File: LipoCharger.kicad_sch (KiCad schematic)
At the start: 10 parts, among them U1 TP4056-42-ESOP8

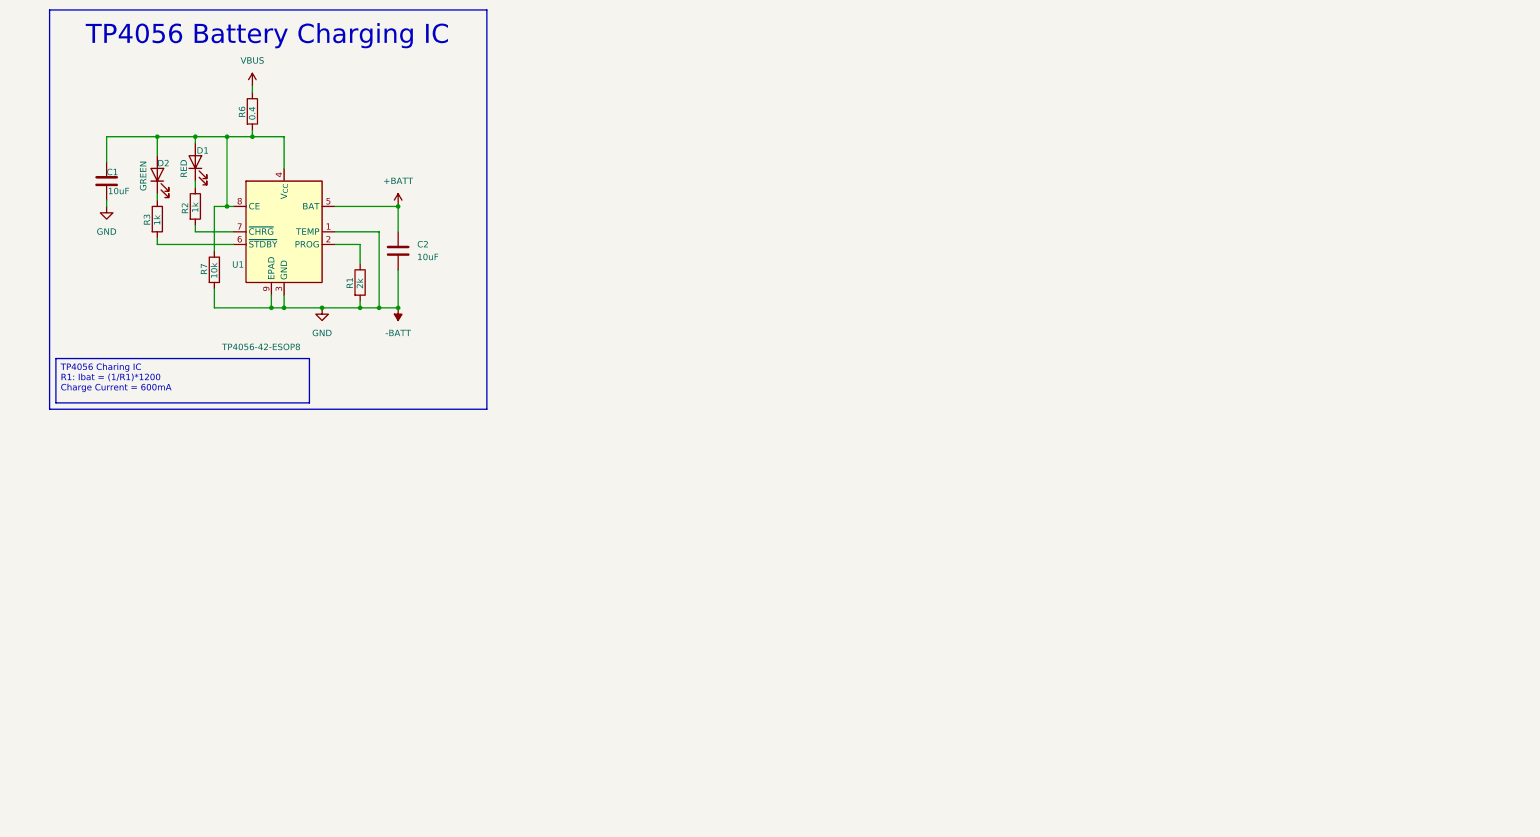
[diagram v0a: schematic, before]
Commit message: Added the DW01 Battery Protection IC and started adding the USB-C port
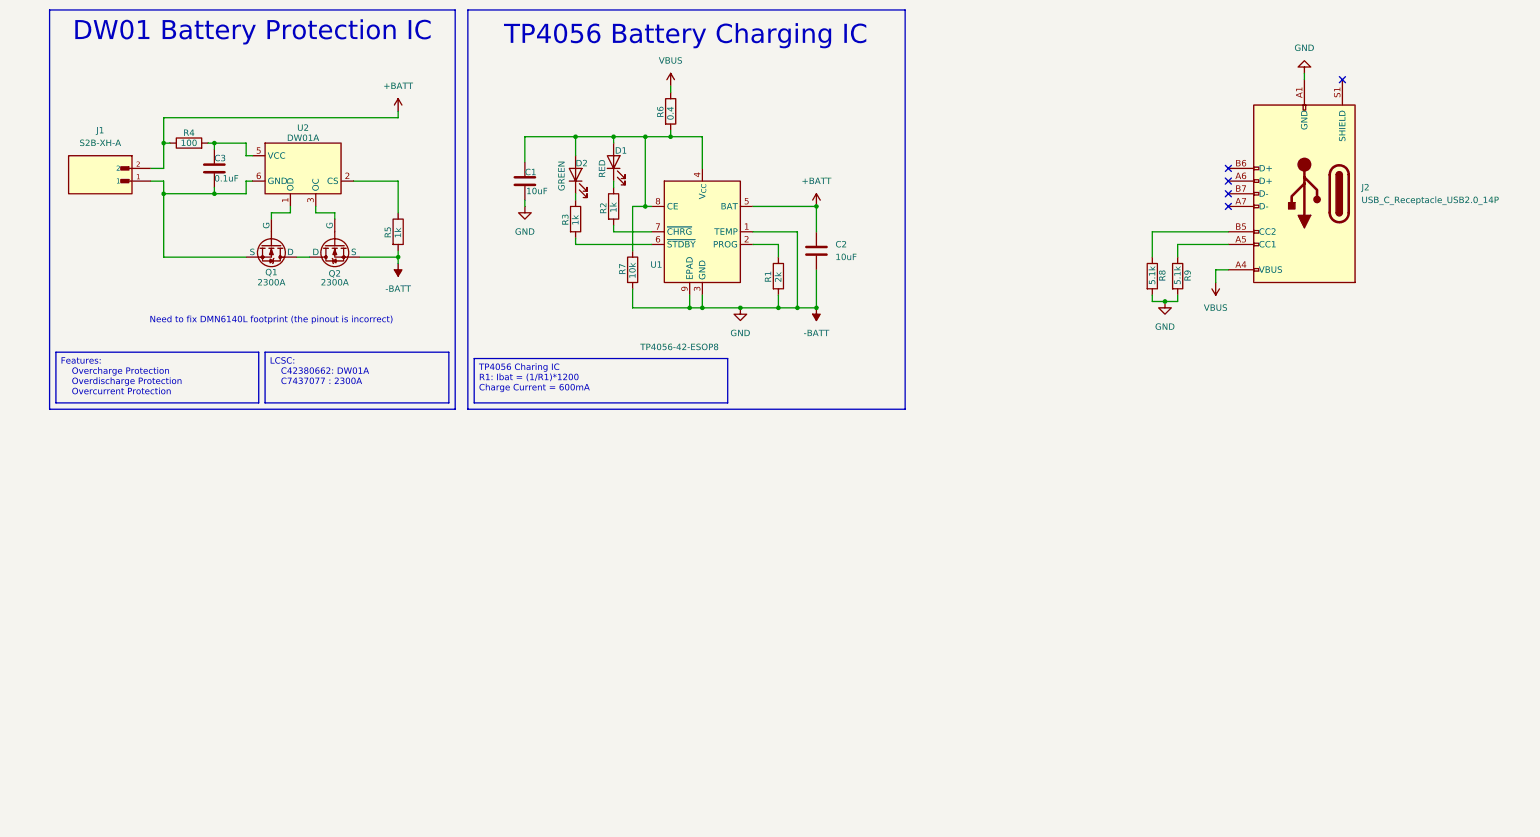
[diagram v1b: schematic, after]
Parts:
- added C3: 0.1uF, Capacitor_SMD:C_0805_2012Metric_Pad1.18x1.45mm_HandSolder, symbol Device:C
- added J1: S2B-XH-A, a_Library:JST_S2B-XH-A, symbol JST_XH:S2B-XH-A
- added J2: USB_C_Receptacle_USB2.0_14P, a_Library:Usb-C, symbol Connector:USB_C_Receptacle_USB2.0_14P
- added Q1, Q2: 2300A, Package_TO_SOT_SMD:SOT-23_Handsoldering, symbol Simulation_SPICE:NMOS
- added R4: 100, Resistor_SMD:R_0805_2012Metric_Pad1.20x1.40mm_HandSolder, symbol Device:R
- added R5: 1k, Resistor_SMD:R_0805_2012Metric_Pad1.20x1.40mm_HandSolder, symbol Device:R
- added R8, R9: 5.1k, Resistor_SMD:R_0805_2012Metric_Pad1.20x1.40mm_HandSolder, symbol Device:R
- added U2: DW01A, Package_TO_SOT_SMD:SOT-23-6, symbol Battery_Management:DW01A
- C1, C2: footprint (none) -> Capacitor_SMD:C_0805_2012Metric_Pad1.18x1.45mm_HandSolder
- R1, R2, R3, R6, R7: footprint (none) -> Resistor_SMD:R_0805_2012Metric_Pad1.20x1.40mm_HandSolder
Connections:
- net +BATT: now also J1.2, R4.1
- net -BATT: now also J2.A1 (GND), J2.A12 (GND), J2.B1 (GND), J2.B12 (GND), Q2.3 (S), R5.2, R8.2, R9.2
- net VBUS: now also J2.A4 (VBUS), J2.A9 (VBUS), J2.B4 (VBUS), J2.B9 (VBUS)
- new net: Q1.1 (D), Q2.1 (D)
- new net: Q2.2 (G), U2.3 (OC)
- new net: C3.2, J1.1, Q1.3 (S), U2.6 (GND)
- new net: C3.1, R4.2, U2.5 (VCC)
- new net: J2.B5 (CC2), R8.1
- new net: J2.A5 (CC1), R9.1
- new net: Q1.2 (G), U2.1 (OD)
- new net: R5.1, U2.2 (CS)
- no-connect marks 0 -> 5
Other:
- note added: "DW01 Battery Protection IC"
- note added: "Need to fix DMN6140L footprint (the pinout is incorrect)"
- moved on the sheet: C1, C2, D1, D2, R1, R2, R3, R6, R7, U1

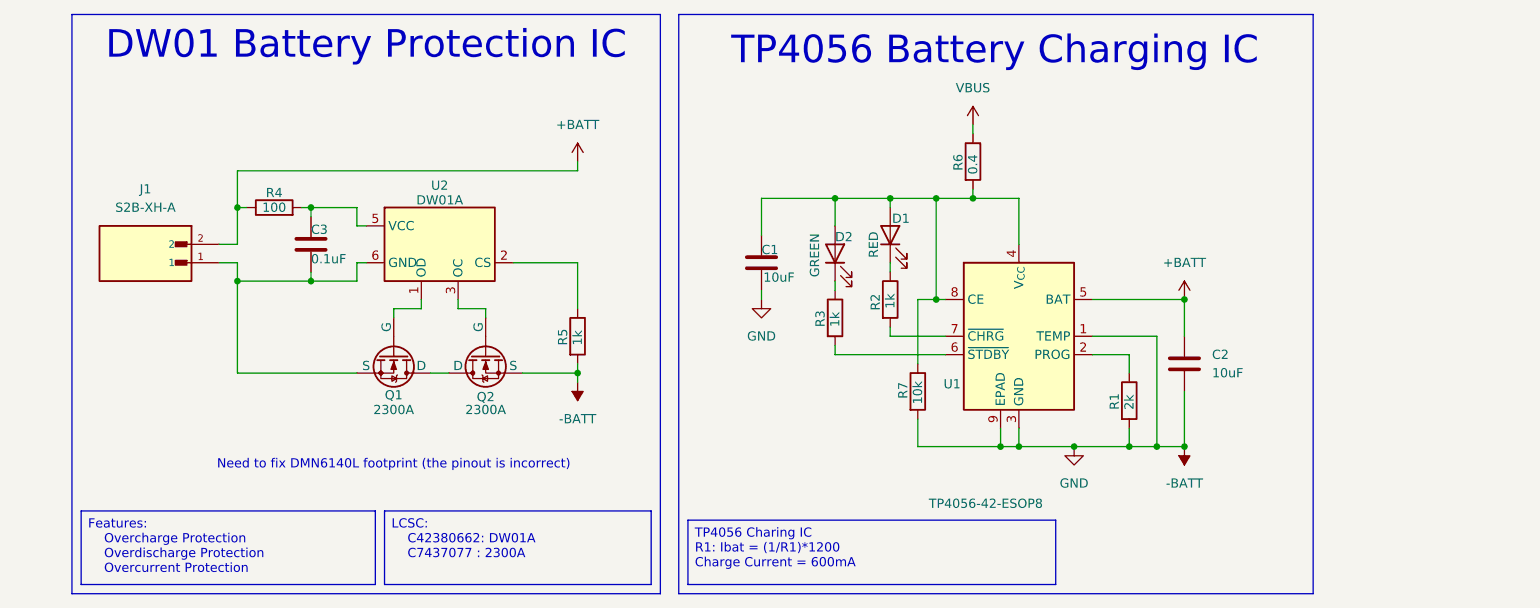
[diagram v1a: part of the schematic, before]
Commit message: Replaced the DW01 with a FM2113
The DW01 was not suited for a LIPO battery, the under voltage threshold was too low, so it was replaced with the FM2113 which has a much higher threshold
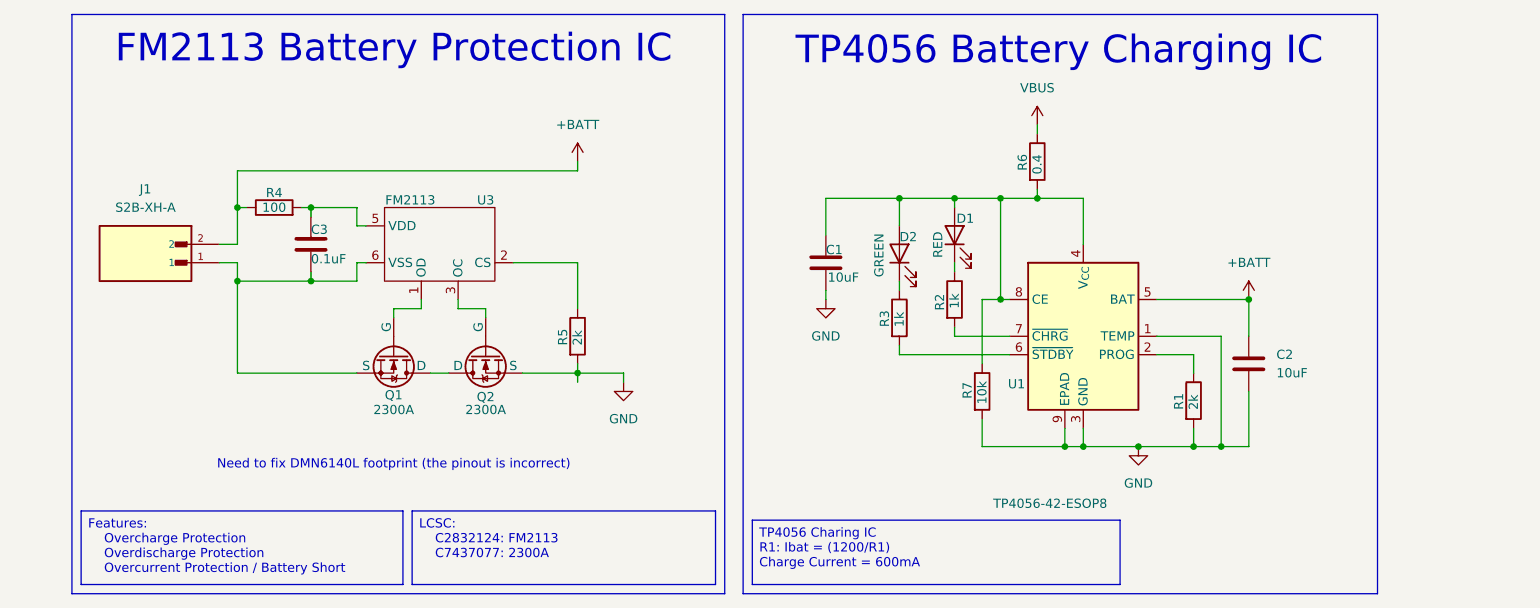
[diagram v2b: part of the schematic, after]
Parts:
- removed U2: DW01A, Package_TO_SOT_SMD:SOT-23-6, symbol Battery_Management:DW01A
- added U3: FM2113, Package_TO_SOT_SMD:TSOT-23-6_HandSoldering, symbol New_Library:FM2113
- R5: value 1k -> 2k
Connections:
- net at Q2.2 (G): now also U3.3 (OC)
- net at C3.2, J1.1, Q1.3 (S): now also U3.6 (VSS)
- net at C3.1, R4.2: now also U3.5 (VDD)
- net at Q1.2 (G): now also U3.1 (OD)
- net at R5.1: now also U3.2 (CS)
- net -BATT renamed GND
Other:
- note added: "FM2113 Battery Protection IC"
- note removed: "DW01 Battery Protection IC"
- moved on the sheet: C1, C2, D1, D2, R1, R2, R3, R6, R7, U1

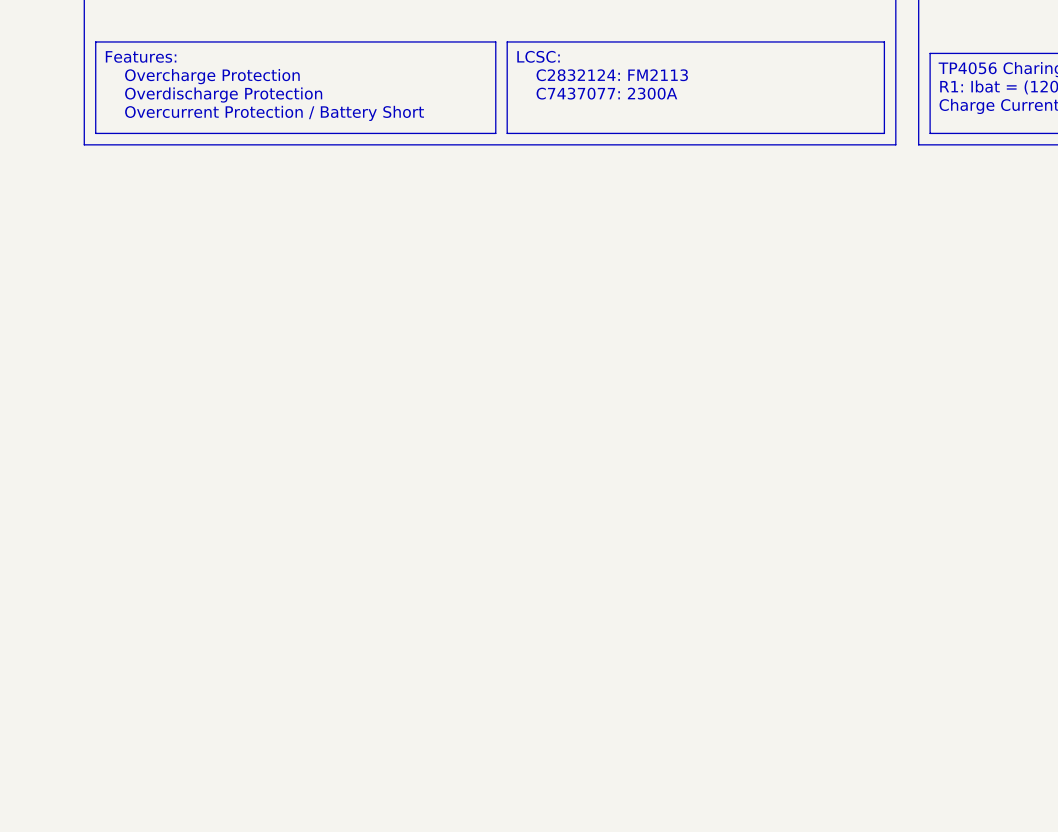
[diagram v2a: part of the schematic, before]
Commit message: Updated usb-c connector, added the 5v switcher, and started to find specific components for the swithcher
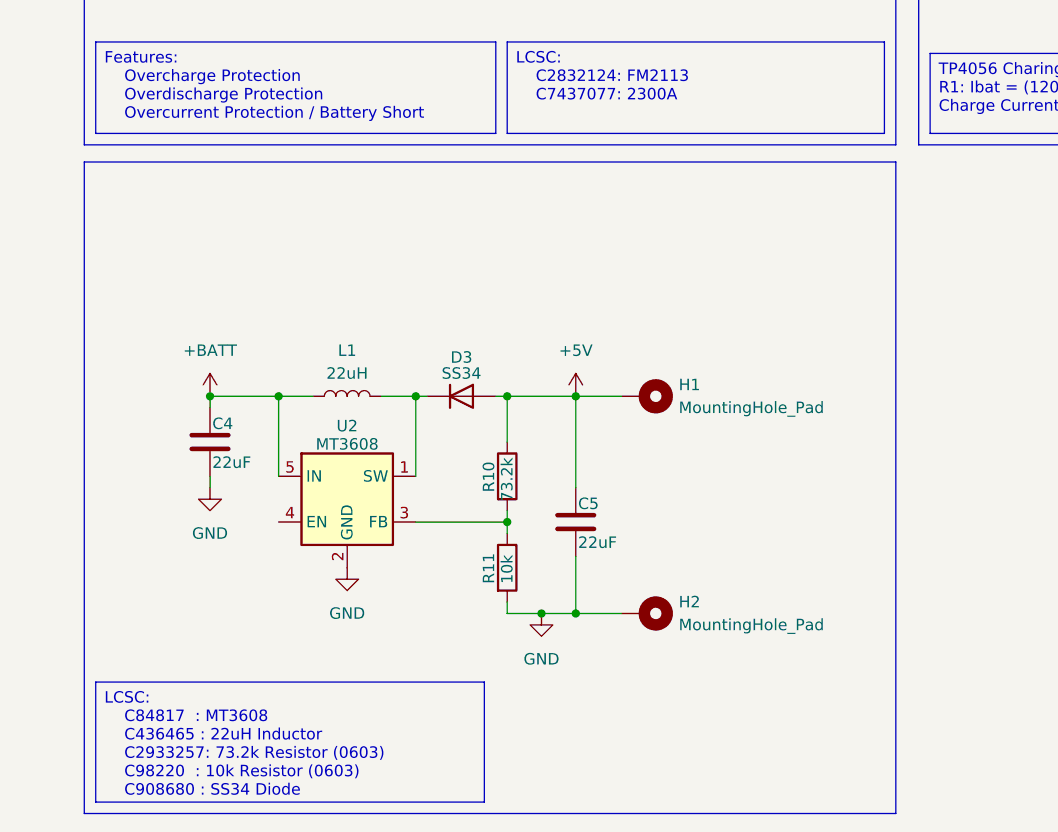
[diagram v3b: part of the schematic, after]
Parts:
- added C4, C5: 22uF, Capacitor_SMD:C_0603_1608Metric_Pad1.08x0.95mm_HandSolder, symbol Device:C
- added D3: SS34, Diode_SMD:D_SMA-SMB_Universal_Handsoldering, symbol Device:D
- added H1, H2: MountingHole_Pad, MountingHole:MountingHole_2.2mm_M2_DIN965_Pad, symbol Mechanical:MountingHole_Pad
- added L1: 22uH, symbol Device:L
- added R10: 73.2k, Resistor_SMD:R_0603_1608Metric_Pad0.98x0.95mm_HandSolder, symbol Device:R
- added R11: 10k, Resistor_SMD:R_0603_1608Metric_Pad0.98x0.95mm_HandSolder, symbol Device:R
- added U2: MT3608, Package_TO_SOT_SMD:SOT-23-6, symbol Regulator_Switching:MT3608
- C1, C2, C3: footprint Capacitor_SMD:C_0805_2012Metric_Pad1.18x1.45mm_HandSolder -> Capacitor_SMD:C_0603_1608Metric_Pad1.08x0.95mm_HandSolder
- D1, D2: footprint (none) -> LED_SMD:LED_0603_1608Metric_Pad1.05x0.95mm_HandSolder
- R1, R2, R3, R4, R5, R6, R7, R8, R9: footprint Resistor_SMD:R_0805_2012Metric_Pad1.20x1.40mm_HandSolder -> Resistor_SMD:R_0603_1608Metric_Pad0.98x0.95mm_HandSolder
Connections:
- net +BATT: now also C4.1, L1.1, U2.5 (IN)
- net GND: now also C4.2, C5.2, H2.1, R11.2, U2.2 (GND)
- new net: D3.1 (K), L1.2, U2.1 (SW)
- new net: R10.2, R11.1, U2.3 (FB)
- new net +5V: C5.1, D3.2 (A), H1.1, R10.1

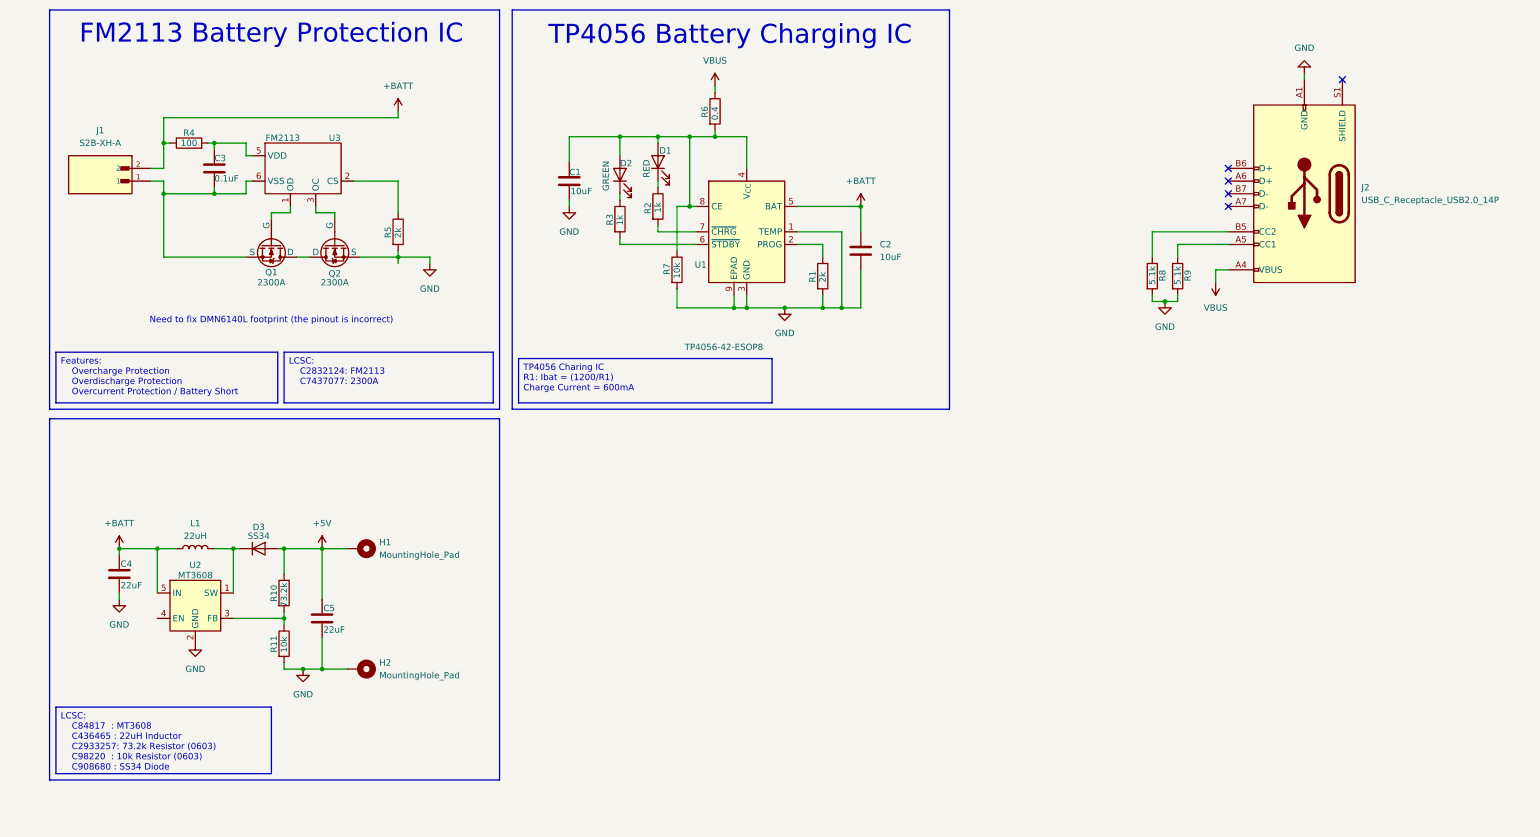
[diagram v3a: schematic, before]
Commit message: Cleaned up schematic and added a slide switch
* Added a slide switch for enabling the 5v Switcher
* Added the USB protection and part numbers
* Consolidated all of the symbols into the Symbols folder (instead of the _Library.pretty folder)
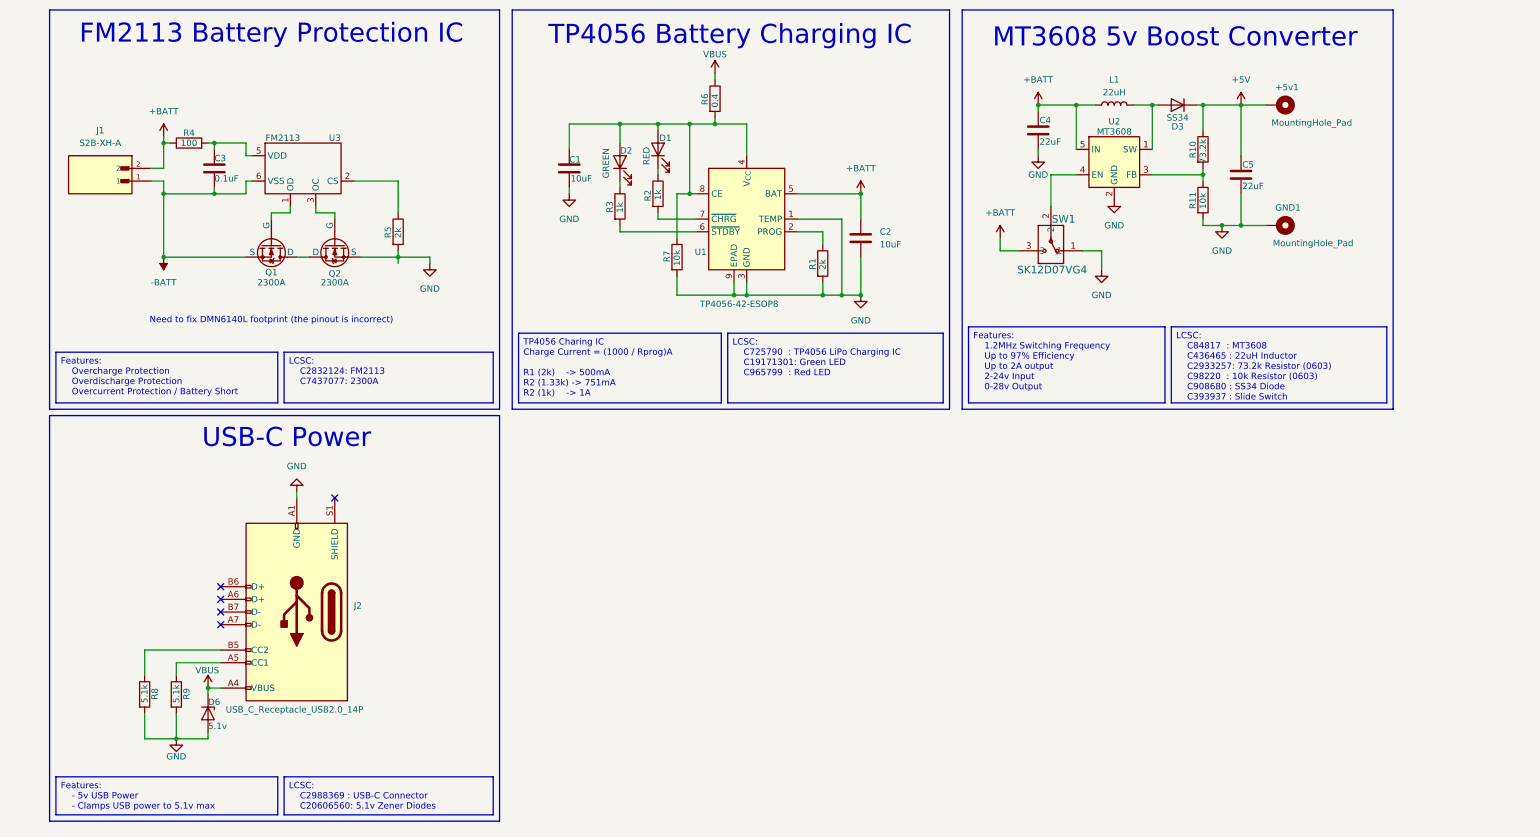
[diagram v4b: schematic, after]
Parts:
- added D6: 5.1v, Diode_SMD:Nexperia_CFP3_SOD-123W, symbol Device:D_Zener
- added SW1: SK12D07VG4, a_Library:SK12D07VG4 - (SlideSwitch), symbol SlideSwitch:OS102011MA1QN1
- renumbered H1 to +5v1, H2 to GND1
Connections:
- net +5V: now also D3.1 (K); no longer D3.2 (A)
- net +BATT: now also SW1.3
- net GND: now also D6.2 (A), SW1.1
- net VBUS: now also D6.1 (K)
- net -BATT: now reaches C3.2, J1.1, Q1.3 (S), U3.6 (VSS)
- net at L1.2, U2.1 (SW): now also D3.2 (A); no longer D3.1 (K)
- net at U2.4 (EN): now also SW1.2
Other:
- note added: "MT3608 5v Boost Converter"
- note added: "USB-C Power"
- moved on the sheet: +5v1, C1, C2, C4, C5, D1, D2, D3, GND1, J2, L1, R1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
